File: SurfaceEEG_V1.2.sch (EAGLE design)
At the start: 70 parts, among them IC1 LMV602, IC2 TSZ124IQ4T, U1 MCP4442-103E/ST

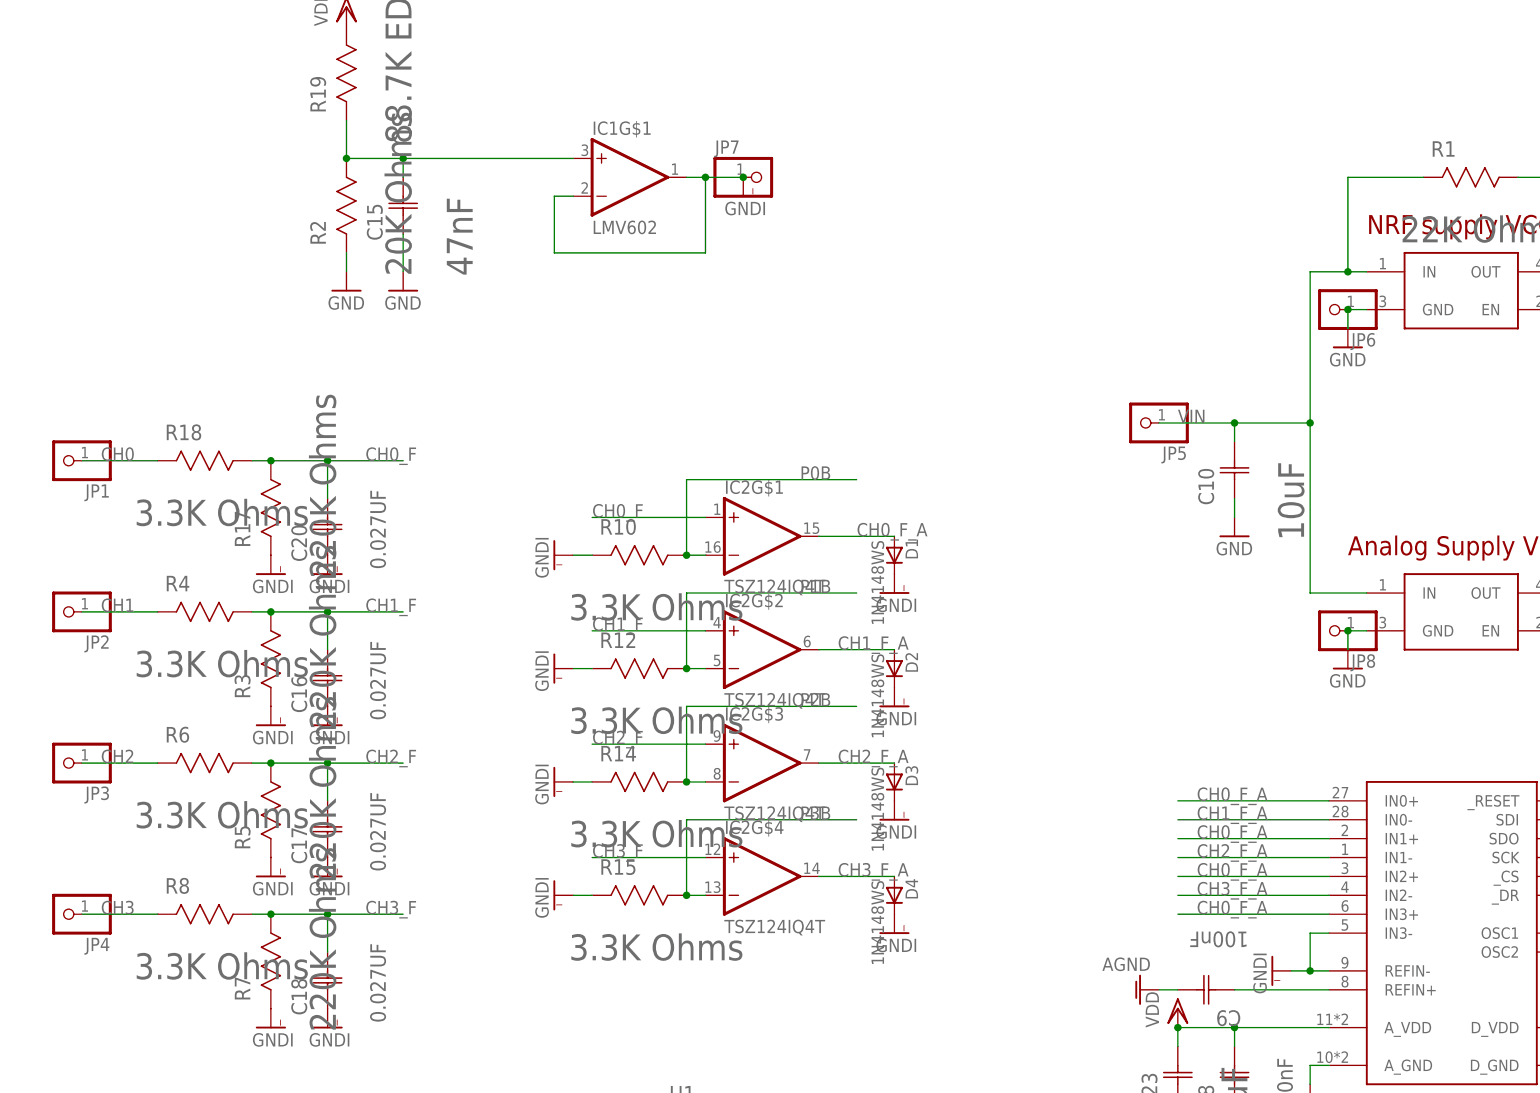
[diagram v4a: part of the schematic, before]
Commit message: Finished PCB and updated schematics
Added headers for sensor board connection and placed/routed remaining caps, optimized everything
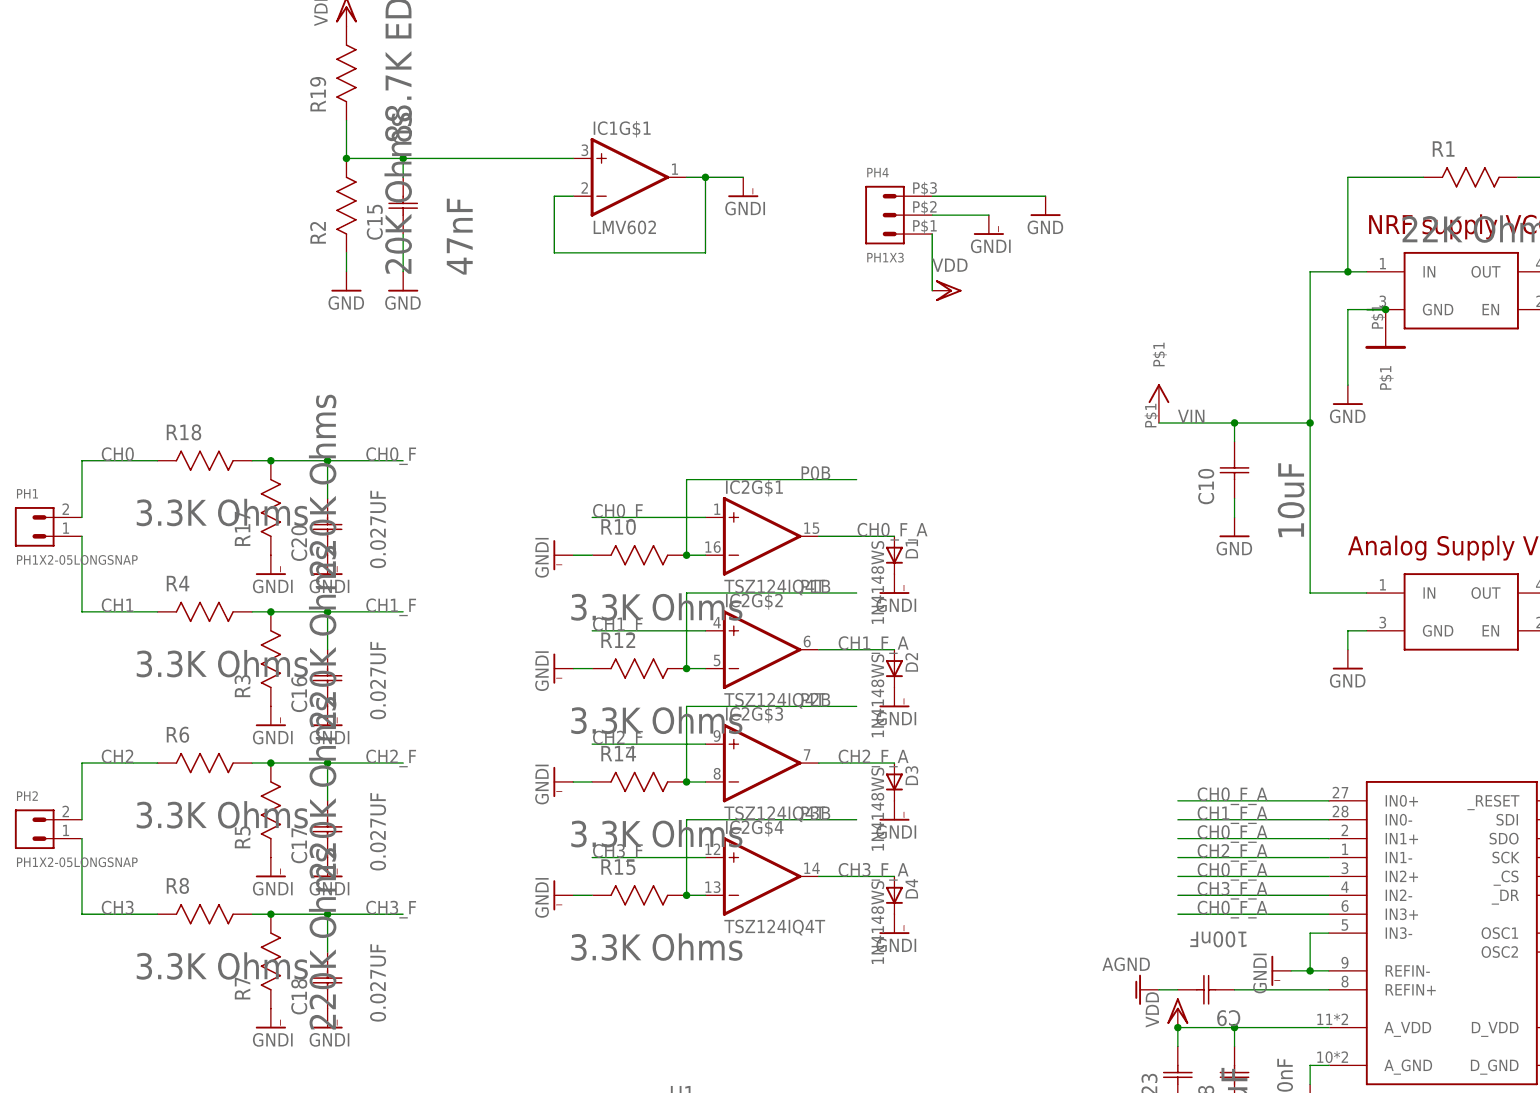
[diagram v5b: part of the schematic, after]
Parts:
- removed JP1, JP2, JP3, JP4, JP5, JP6, JP7, JP8: (no value), adafruit:PINHD-1X1
- added PH1, PH2: PH1X2-05LONGSNAP, pel_hdr:PH1X2-05LONGSNAP
- added PH4: PH1X3, (misc)-parts-that-we-use:PH1X3
- added U$4: VCC, (custom)-new-components:VCC
- added U$5: GND, (custom)-new-components:GND
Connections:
- net CH0: now also PH1.2; no longer JP1.1
- net CH1: now also PH1.1; no longer JP2.1
- net CH2: now also PH2.2; no longer JP3.1
- net CH3: now also PH2.1; no longer JP4.1
- net GND: now also PH4.3, U$5.P$1; no longer JP6.1, JP8.1
- net GNDI: now also PH4.2; no longer JP7.1
- net VDD: now also PH4.1
- net VIN: now also U$4.P$1; no longer JP5.1
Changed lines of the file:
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@@
 <?xml version="1.0" encoding="utf-8"?>
 <!DOCTYPE eagle SYSTEM "eagle.dtd">
-<eagle version="7.5.0">
+<eagle version="7.7.0">
 <drawing>
 <settings>
@@
 <layer number="49" name="Reference" color="7" fill="1" visible="no" active="no"/>
 <layer number="50" name="dxf" color="7" fill="1" visible="no" active="no"/>
-<layer number="51" name="tDocu" color="6" fill="1" visible="no" active="no"/>
+<layer number="51" name="tDocu" color="7" fill="1" visible="no" active="no"/>
 <layer number="52" name="bDocu" color="7" fill="1" visible="no" active="no"/>
 <layer number="53" name="tGND_GNDA" color="7" fill="9" visible="no" active="no"/>
@@
 <layer number="59" name="tCarbon" color="7" fill="1" visible="no" active="no"/>
 <layer number="60" name="bCarbon" color="7" fill="1" visible="no" active="no"/>
+<layer number="61" name="stand" color="7" fill="1" visible="no" active="no"/>
 <layer number="90" name="Modules" color="5" fill="1" visible="yes" active="yes"/>
 <layer number="91" name="Nets" color="2" fill="1" visible="yes" active="yes"/>
@@
 <layer number="128" name="_bValues" color="7" fill="1" visible="yes" active="yes"/>
 <layer number="129" name="Mask" color="7" fill="1" visible="yes" active="yes"/>
+<layer number="130" name="bLogo" color="7" fill="1" visible="yes" active="yes"/>
 <layer number="131" name="tAdjust" color="7" fill="1" visible="yes" active="yes"/>
 <layer number="132" name="bAdjust" color="7" fill="1" visible="yes" active="yes"/>
@@
 <part name="GNDI17" library="supply1" deviceset="GNDI" device=""/>
 <part name="GNDI18" library="supply1" deviceset="GNDI" device=""/>
-<part name="JP1" library="adafruit" deviceset="PINHD-1X1" device=""/>
-<part name="JP2" library="adafruit" deviceset="PINHD-1X1" device=""/>
-<part name="JP3" library="adafruit" deviceset="PINHD-1X1" device=""/>
-<part name="JP4" library="adafruit" deviceset="PINHD-1X1" device=""/>
-<part name="JP5" library="adafruit" deviceset="PINHD-1X1" device=""/>
-<part name="JP6" library="adafruit" deviceset="PINHD-1X1" device=""/>
-<part name="JP7" library="adafruit" deviceset="PINHD-1X1" device=""/>
-<part name="JP8" library="adafruit" deviceset="PINHD-1X1" device=""/>
+<part name="PH1" library="pel_hdr" deviceset="PH1X2" device="-05LONGSNAP"/>
+<part name="PH2" library="pel_hdr" deviceset="PH1X2" device="-05LONGSNAP"/>
+<part name="U$4" library="(custom)-new-components" deviceset="VCC" device=""/>
+<part name="U$5" library="(custom)-new-components" deviceset="GND" device=""/>
+<part name="GND26" library="supply1" deviceset="GND" device=""/>
+<part name="GNDI19" library="supply1" deviceset="GNDI" device=""/>
+<part name="VDD7" library="supply1" deviceset="VDD" device=""/>
+<part name="PH4" library="(misc)-parts-that-we-use" deviceset="PH1X3" device=""/>
 </parts>
 <sheets>
@@
 <instance part="GND3" gate="1" x="71.12" y="73.66"/>
 <instance part="GND4" gate="1" x="88.9" y="68.58"/>
-<instance part="GND5" gate="1" x="40.64" y="175.26"/>
+<instance part="GND5" gate="1" x="40.64" y="167.64"/>
 <instance part="GND6" gate="1" x="25.4" y="149.86"/>
 <instance part="GND7" gate="1" x="91.44" y="175.26"/>
@@
 <instance part="GNDI17" gate="G$1" x="-20.32" y="96.52"/>
 <instance part="GNDI18" gate="G$1" x="30.48" y="91.44" rot="R270"/>
-<instance part="JP1" gate="G$1" x="-132.08" y="160.02" rot="R180"/>
-<instance part="JP2" gate="G$1" x="-132.08" y="139.7" rot="R180"/>
-<instance part="JP3" gate="G$1" x="-132.08" y="119.38" rot="R180"/>
-<instance part="JP4" gate="G$1" x="-132.08" y="99.06" rot="R180"/>
-<instance part="JP5" gate="G$1" x="12.7" y="165.1" rot="R180"/>
-<instance part="JP6" gate="G$1" x="38.1" y="180.34" rot="R180"/>
-<instance part="JP7" gate="G$1" x="-38.1" y="198.12"/>
-<instance part="JP8" gate="G$1" x="38.1" y="137.16" rot="R180"/>
+<instance part="PH1" gate="G$1" x="-137.16" y="149.86"/>
+<instance part="PH2" gate="G$1" x="-137.16" y="109.22"/>
+<instance part="U$4" gate="G$1" x="15.24" y="170.18"/>
+<instance part="U$5" gate="G$1" x="45.72" y="175.26"/>
+<instance part="GND26" gate="1" x="0" y="193.04"/>
+<instance part="GNDI19" gate="G$1" x="-7.62" y="190.5"/>
+<instance part="VDD7" gate="G$1" x="-12.7" y="182.88" rot="R270"/>
+<instance part="PH4" gate="G$1" x="-22.86" y="190.5"/>
 </instances>
 <busses>
@@
 <segment>
 <pinref part="GND5" gate="1" pin="GND"/>
-<wire x1="43.18" y1="180.34" x2="40.64" y2="180.34" width="0.1524" layer="91"/>
-<wire x1="40.64" y1="180.34" x2="40.64" y2="177.8" width="0.1524" layer="91"/>
+<wire x1="45.72" y1="180.34" x2="40.64" y2="180.34" width="0.1524" layer="91"/>
+<wire x1="40.64" y1="180.34" x2="40.64" y2="170.18" width="0.1524" layer="91"/>
 <pinref part="U$1" gate="G$1" pin="GND"/>
-<pinref part="JP6" gate="G$1" pin="1"/>
-<junction x="40.64" y="180.34"/>
+<pinref part="U$5" gate="G$1" pin="P$1"/>
+<junction x="45.72" y="180.34"/>
+<wire x1="45.72" y1="180.34" x2="43.18" y2="180.34" width="0.1524" layer="91"/>
 </segment>
 <segment>
@@
 <wire x1="40.64" y1="137.16" x2="43.18" y2="137.16" width="0.1524" layer="91"/>
 <pinref part="U$2" gate="G$1" pin="GND"/>
-<pinref part="JP8" gate="G$1" pin="1"/>
-<junction x="40.64" y="137.16"/>
 </segment>
 <segment>
@@
 <pinref part="C27" gate="A" pin="C1"/>
 <wire x1="-81.28" y1="66.04" x2="-86.36" y2="66.04" width="0.1524" layer="91"/>
+</segment>
+<segment>
+<pinref part="GND26" gate="1" pin="GND"/>
+<wire x1="-15.24" y1="195.58" x2="0" y2="195.58" width="0.1524" layer="91"/>
+<pinref part="PH4" gate="G$1" pin="3"/>
 </segment>
 </net>
@@
 <pinref part="C10" gate="A" pin="C2"/>
 <pinref part="R1" gate="A" pin="R2"/>
-<pinref part="JP5" gate="G$1" pin="1"/>
+<pinref part="U$4" gate="G$1" pin="P$1"/>
 </segment>
 </net>
@@
 <label x="-127" y="99.06" size="1.778" layer="95"/>
 <pinref part="R8" gate="A" pin="R2"/>
-<pinref part="JP4" gate="G$1" pin="1"/>
+<pinref part="PH2" gate="G$1" pin="1"/>
+<wire x1="-129.54" y1="99.06" x2="-129.54" y2="109.22" width="0.1524" layer="91"/>
 </segment>
 </net>
@@
 <wire x1="-119.38" y1="160.02" x2="-129.54" y2="160.02" width="0.1524" layer="91"/>
 <label x="-127" y="160.02" size="1.778" layer="95"/>
-<pinref part="JP1" gate="G$1" pin="1"/>
 <pinref part="R18" gate="A" pin="R2"/>
+<pinref part="PH1" gate="G$1" pin="2"/>
+<wire x1="-129.54" y1="160.02" x2="-129.54" y2="152.4" width="0.1524" layer="91"/>
 </segment>
 </net>
@@
 <label x="-127" y="139.7" size="1.778" layer="95"/>
 <pinref part="R4" gate="A" pin="R2"/>
-<pinref part="JP2" gate="G$1" pin="1"/>
+<pinref part="PH1" gate="G$1" pin="1"/>
+<wire x1="-129.54" y1="139.7" x2="-129.54" y2="149.86" width="0.1524" layer="91"/>
 </segment>
 </net>
@@
 <label x="-127" y="119.38" size="1.778" layer="95"/>
 <pinref part="R6" gate="A" pin="R2"/>
-<pinref part="JP3" gate="G$1" pin="1"/>
+<pinref part="PH2" gate="G$1" pin="2"/>
+<wire x1="-129.54" y1="119.38" x2="-129.54" y2="111.76" width="0.1524" layer="91"/>
 </segment>
 </net>
@@
 <pinref part="R19" gate="A" pin="R1"/>
 </segment>
+<segment>
+<pinref part="VDD7" gate="G$1" pin="VDD"/>
+<wire x1="-15.24" y1="190.5" x2="-15.24" y2="182.88" width="0.1524" layer="91"/>
+<pinref part="PH4" gate="G$1" pin="1"/>
+</segment>
 </net>
 <net name="GNDI" class="0">
@@
 <pinref part="IC1" gate="G$1" pin="IN-"/>
 <pinref part="IC1" gate="G$1" pin="OUT"/>
-<pinref part="JP7" gate="G$1" pin="1"/>
-<junction x="-40.64" y="198.12"/>
 </segment>
 <segment>
@@
 <pinref part="GNDI18" gate="G$1" pin="GNDI"/>
 </segment>
-</net>
+<segment>
+<pinref part="GNDI19" gate="G$1" pin="GNDI"/>
+<wire x1="-15.24" y1="193.04" x2="-7.62" y2="193.04" width="0.1524" layer="91"/>
+<pinref part="PH4" gate="G$1" pin="2"/>
+</segment>
+</net>
